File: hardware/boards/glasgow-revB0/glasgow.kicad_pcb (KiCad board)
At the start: 4 copper layers, 80 x 49 mm, 124 parts, among them J1 USB_B_Micro, J2 Conn_02x10_Odd_Even, J3 Conn_02x10_Odd_Even, J4 Conn_01x02, U1 CY7C68013A-56LTX, U10 DAC081C081CIMK, U11 TPS73101DBV, U12 ADC081C021CIMM, U13 DAC081C081CIMK, U14 TPS73101DBV, U15 TPD3S014, U2 CAT24M01W, U3 CAT24C256W, U4 ICE40UP5K-SG48ITR, U5 FXMA108BQX, U6 FXMA108BQX, U7 LM3880MF-1AF, U8 MIC5355-S4YMME, U9 ADC081C021CIMM, Y1 24M

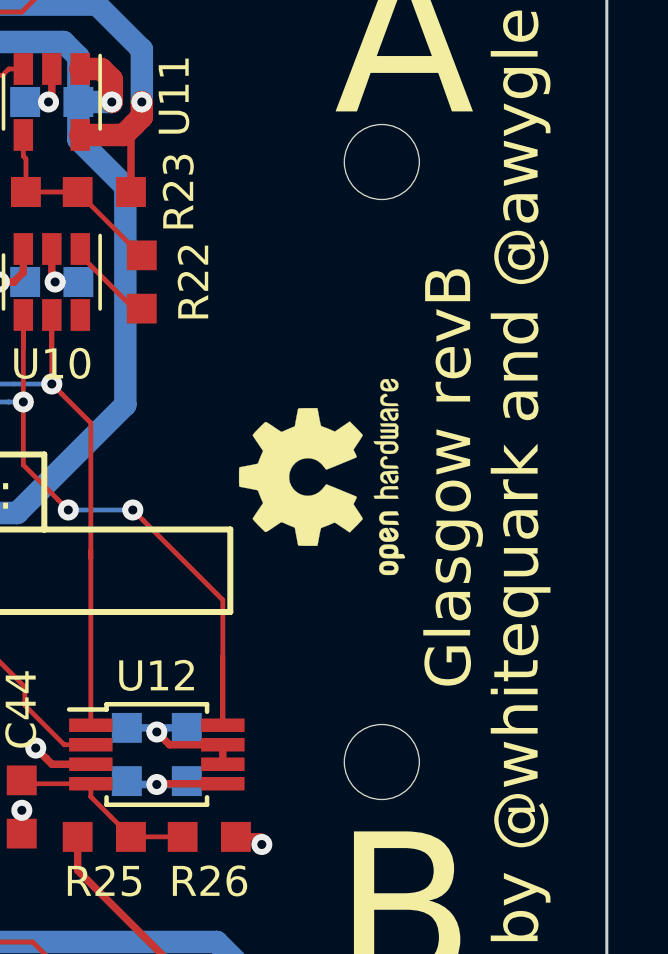
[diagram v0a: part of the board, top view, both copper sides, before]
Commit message: Updated revB0 to KiCad V5 and bumped revision from B to B0.
Also added bit more information to the board layout sheet legend.
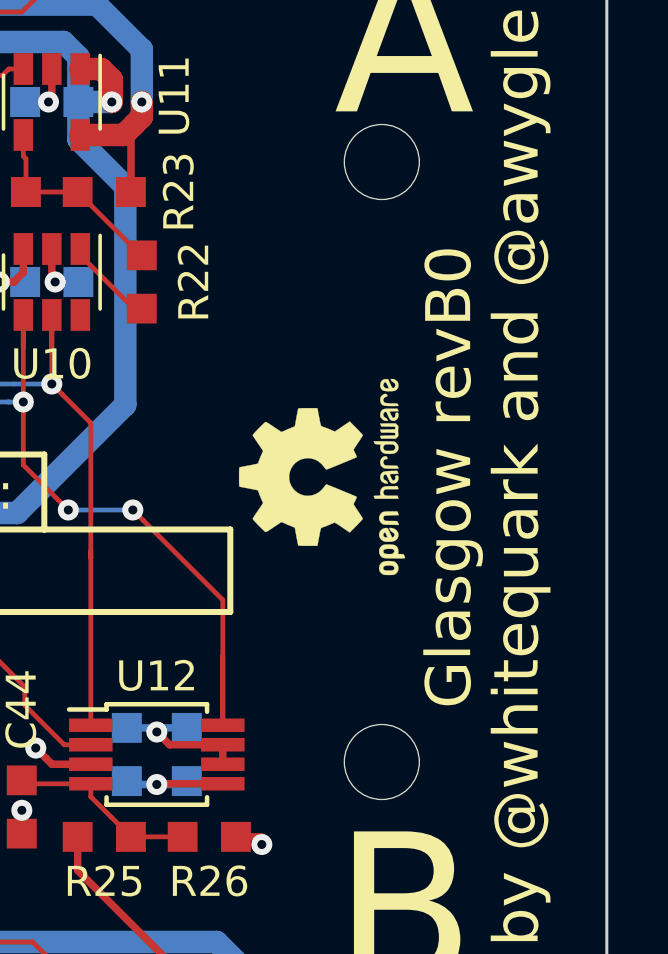
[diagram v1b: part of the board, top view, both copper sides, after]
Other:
- board text added: "Glasgow revB0"
- board text removed: "Glasgow revB"
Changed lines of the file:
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@@
-(kicad_pcb (version 20171130) (host pcbnew 5.0.0-rc3-6a2723a~65~ubuntu18.04.1)
+(kicad_pcb (version 20171130) (host pcbnew 5.0.1-33cea8e~68~ubuntu18.04.1)
   (general
     (thickness 1.6)
@@
   )
   (page A4)
+  (title_block
+    (title "Glasgow Debug Tool")
+    (rev B0)
+    (company "whitequark research")
+    (comment 1 "by @whitequark & @awygle")
+  )
   (layers
     (0 F.Cu signal)
@@
     (effects (font (size 1.5 1.5) (thickness 0.15)))
   )
-  (gr_text "Glasgow revB" (at 124.75 95.5 90) (layer F.SilkS)
+  (gr_text "Glasgow revB0" (at 124.75 95.5 90) (layer F.SilkS)
     (effects (font (size 1.5 1.5) (thickness 0.15)))
   )
